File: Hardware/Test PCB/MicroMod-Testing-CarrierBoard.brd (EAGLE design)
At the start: 85.1 x 43.2 mm, 139 parts, among them J11 microSD, J12 SPI, J13 QWIIC_RIGHT_ANGLE, J15 Dedicated, J2 JTAG, J3 QWIIC_RIGHT_ANGLE, J6 MICROMOD-2222-C, J8 Dedicated, U2 MCP73831, U5 AP7361C-33

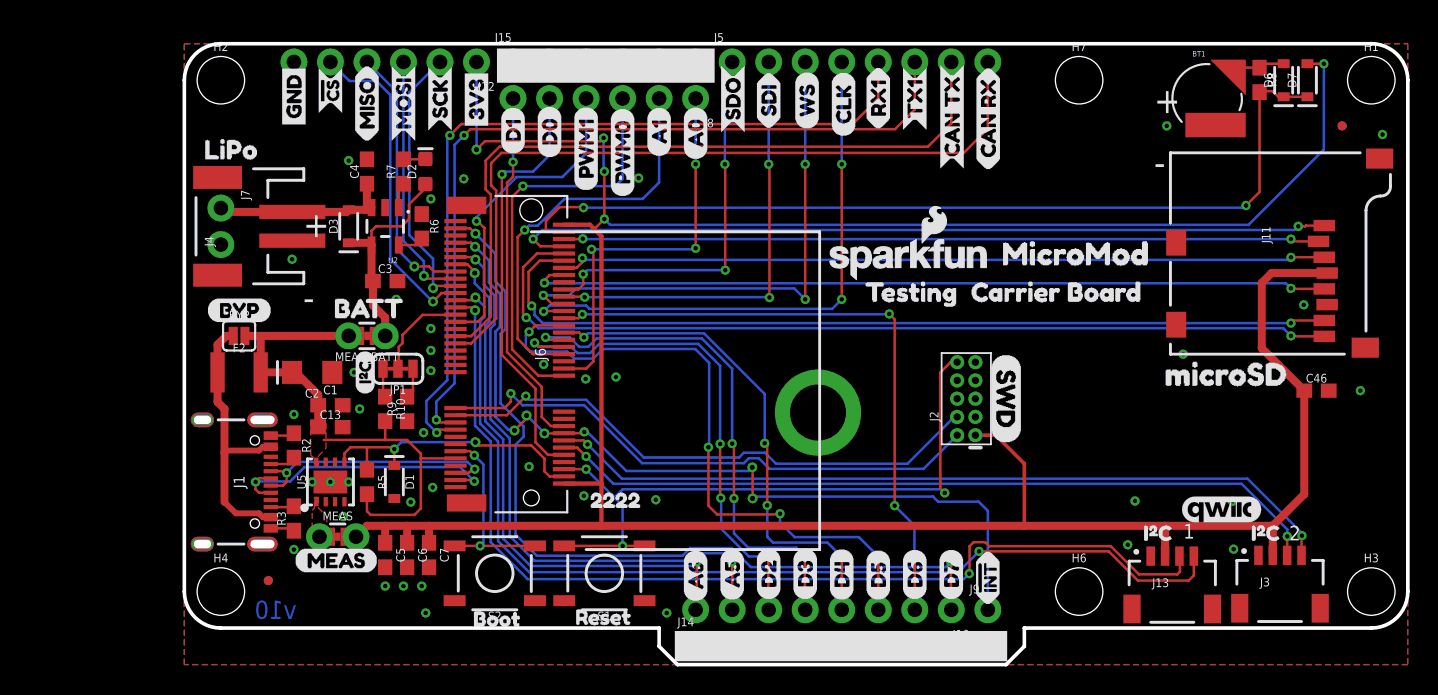
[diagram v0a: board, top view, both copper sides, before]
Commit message: Updates testing carrier board with all nets added and half of teh new ones added
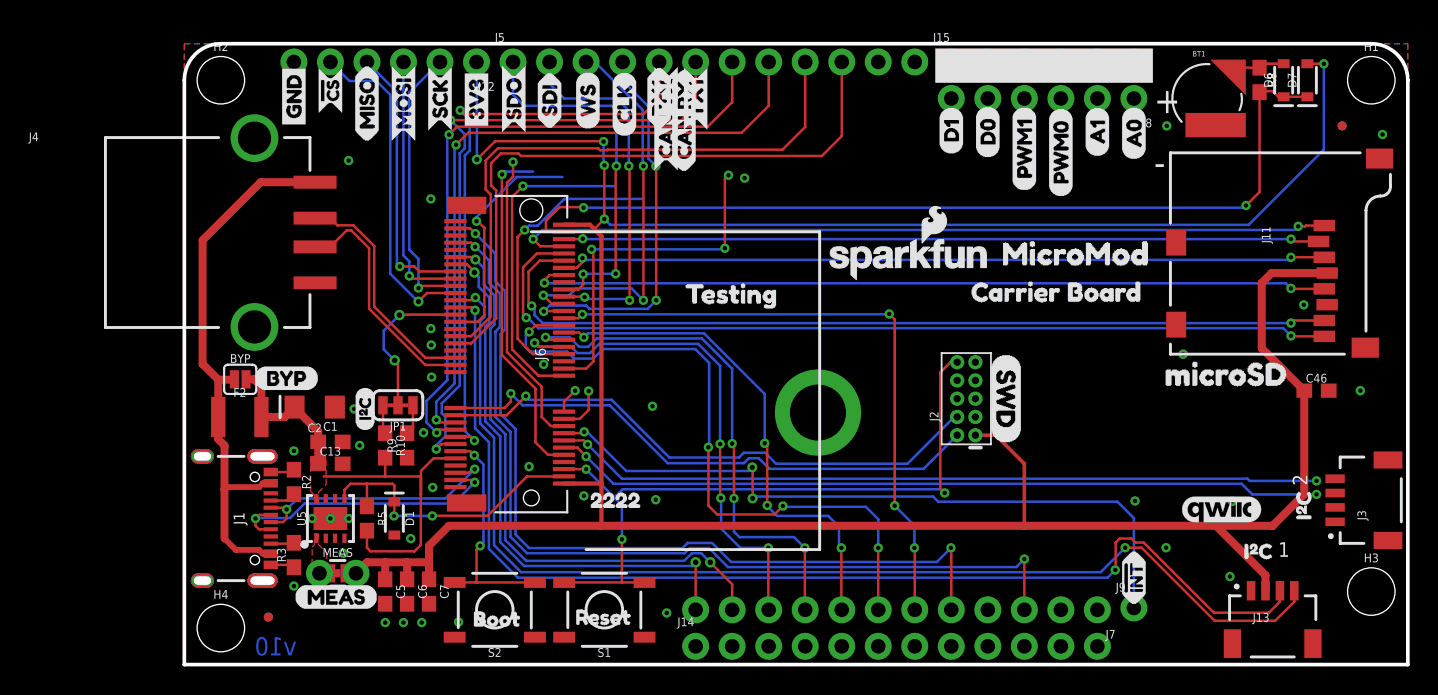
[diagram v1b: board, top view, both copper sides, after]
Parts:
- removed C3, C4: 4.7uF, SparkFun-Capacitors:0603
- removed D2: Yellow, SparkFun-LED:LED-0603
- removed D3: 3A/10V/280mV, SparkFun-DiscreteSemi:SOD-323
- removed H6, H7: STAND-OFF, SparkFun-Hardware:STAND-OFF
- removed J10: (no value), SparkFun-Connectors:1X08_NO_SILK
- removed MEAS_BATT: (no value), SparkFun-Jumpers:COMBO-JUMPER_2_NC_TRACE
- removed R6: 2.2k, SparkFun-Resistors:0603
- removed R7: 1k, SparkFun-Resistors:0603
- removed U$1, U$67: (no value), bottom PTH:A51
- removed U$11, U$69: (no value), bottom PTH:D22
- removed U$17, U$70: (no value), bottom PTH:D33
- removed U$18, U$71: (no value), bottom PTH:D44
- removed U$20, U$72: (no value), bottom PTH:D55
- removed U$3, U$68: (no value), bottom PTH:A60
- removed U$30, U$73: (no value), bottom PTH:D66
- removed U$32, U$74: (no value), bottom PTH:D77
- removed U$33: (no value), buzzard_labels (9):LIPO0
- removed U$56: (no value), buzzard_labels:BATT0
- removed U2: MCP73831, SparkFun-IC-Power:SOT23-5
- J14: device SparkFun-Connectors:1X09_NO_SILK -> SparkFun-Connectors:1X12_NO_SILK
- J4: value (none) -> USB_A_SMT_FEMALE; device SparkFun-Connectors:JST-2-SMD -> SparkFun-Connectors:USB-A-S-SILK-FEMALE
- J5: device SparkFun-Connectors:1X08_NO_SILK -> SparkFun-Connectors:1X12_NO_SILK
- J7: device SparkFun-Connectors:1X02_NO_SILK -> SparkFun-Connectors:1X12_NO_SILK
- moved J7 67.1 mm to (63.5, 3.81), turned to 180 degrees
- moved J15 30.5 mm to (53.3, 41.9)
- moved J8 30.5 mm to (66.0, 39.4)
- moved U$12 30.5 mm to (53.3, 35.4)
- moved U$13 30.5 mm to (53.3, 35.4)
- moved U$14 30.5 mm to (55.9, 35.2)
- moved U$16 30.5 mm to (55.9, 35.2)
- moved U$43 30.5 mm to (66.0, 35.1)
- moved U$44 30.5 mm to (66.0, 35.1)
- moved U$15 30.5 mm to (58.4, 32.9)
- moved U$59 30.5 mm to (61.0, 32.5)
- moved U$60 30.5 mm to (61.0, 32.5)
- moved U$61 30.5 mm to (58.4, 32.9)
- moved U$57 30.5 mm to (63.5, 35.3)
- moved U$58 30.5 mm to (63.5, 35.3)
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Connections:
- net USB_D+ renamed USB_P
- net USB_D- renamed USB_N
- removed net 5V: C3.1, D2.A, D3.C, MEAS_BATT.1, MEAS_BATT.3, U2.4
- removed net A5: J10.7, J6.65
- removed net A6: J10.8, J6.63
- removed net CHG_LED: R7.1, U2.1
- removed net D2: J10.6, J6.40
- removed net D3: J10.5, J6.42
- removed net D4: J10.4, J6.44
- removed net D5: J10.3, J6.46
- removed net D6: J10.2, J6.48
- removed net D7: J10.1, J6.73
- removed net D8/!INT: J6.16, J6.69, J9.1
- removed net N$4: D2.C, R7.2
- removed net N$7: R6.2, U2.5
- removed net V_BATT: C4.1, D3.A, J4.2, J7.1, U2.3
- new net CTS1: J5.5, J6.15
- new net G0: J6.40, J7.10
- new net G1: J6.42, J7.9
- new net G10/ADC_P: J6.63, J7.12
- new net G11: J6.8, J7.1
- new net G2: J6.44, J7.8
- new net G3: J6.46, J7.7
- new net G4: J6.48, J7.6
- new net G5: J6.73, J7.5
- new net G6: J6.71, J7.4
- new net G7: J6.69, J7.3
- new net G8: J6.67, J7.2
- new net G9/ADC_N: J6.65, J7.11
- new net I2C_!INT: J6.16, J9.1
- new net MCLK: J6.58
- new net RTS1: J5.6, J6.13
- new net RX2: J5.12, J6.20
- new net TX2: J5.11, J6.22
- new net USBHOST_N: J4.D-, J6.37
- new net USBHOST_P: J4.D+, J6.35
- net CAN_RXI: now also J5.10; no longer J5.8
- net CAN_TXO: now also J5.9; no longer J5.7
- net GND: now also J14.10, J14.11, J14.12, J4.GND, J4.SHLD1, J4.SHLD2; no longer C3.2, C4.2, J4.1, J7.2, R6.1, U2.2
- net RX1: now also J5.8; no longer J5.6
- net TX1: now also J5.7; no longer J5.5
- net VIN: no longer MEAS_BATT.2, MEAS_BATT.4
- net V_USB: now also J4.VBUS
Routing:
- net G7: track 0.00 -> 63.6 mm, vias 0 -> 2
- net D8/!INT: track 60.7 -> 0.00 mm, vias 7 -> 0
- net G5: track 0.00 -> 60.0 mm, vias 0 -> 2
- net D7: track 59.5 -> 0.00 mm, vias 2 -> 0
- net I2C_!INT: track 0.00 -> 50.0 mm, vias 0 -> 3
- net G3: track 0.00 -> 46.5 mm, vias 0 -> 4
- net RTS1: track 0.00 -> 46.3 mm, vias 0 -> 2
- net D5: track 44.9 -> 0.00 mm, vias 4 -> 0
- net G4: track 0.00 -> 44.0 mm, vias 0 -> 4
- net D6: track 44.0 -> 0.00 mm, vias 4 -> 0
- net A5: track 42.1 -> 0.00 mm, vias 2 -> 0
- net CTS1: track 0.00 -> 42.0 mm, vias 0 -> 2
- net G9/ADC_N: track 0.00 -> 41.3 mm, vias 0 -> 2
- net G10/ADC_P: track 0.00 -> 39.0 mm, vias 0 -> 2
- net A6: track 38.9 -> 0.00 mm, vias 2 -> 0
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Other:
- outline, holes or cut-outs redrawn

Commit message: Finishes routing board
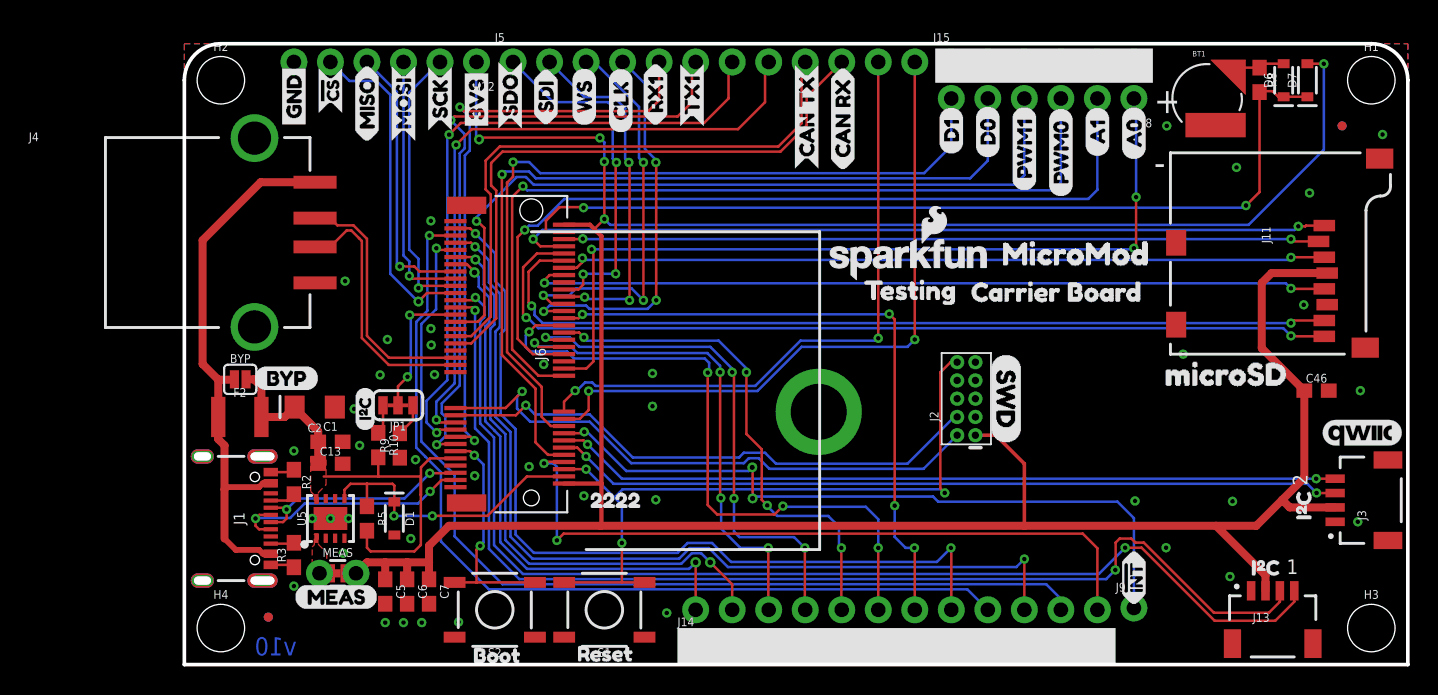
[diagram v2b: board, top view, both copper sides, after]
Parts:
- removed LOGO4: SFE_LOGO_NAME_FLAME.1_INCH, SparkFun-Aesthetics:SFE_LOGO_NAME_FLAME_.1
- removed U$22: (no value), buzzard_labels (9):LOGGING4
- removed U$4: (no value), buzzard_labels (9):DATA3
- moved U$64 38.1 mm to (66.4, 25.7)
- moved U$46 12.4 mm to (46.2, 26.0)
- moved LOGO2 11.1 mm to (81.9, 16.1)
- moved U$34 11.0 mm to (45.8, 34.3)
- moved U$48 11.0 mm to (45.8, 34.3)
- moved U$36 9.78 mm to (43.3, 34.4)
- moved U$54 9.78 mm to (43.3, 34.4)
- moved U$2 2.54 mm to (26.4, 0.76)
- moved H3 2.54 mm to (82.5, 2.54)
- moved U$19 2.54 mm to (19.2, 0.64)
- moved U$75 1.25 mm to (73.3, 6.73)
- moved R9 0.51 mm to (15.0, 15.2)
- moved R10 0.48 mm to (13.5, 15.3)
- moved U$25 0.36 mm to (32.8, 37.5)
- moved U$29 0.36 mm to (32.8, 37.5)
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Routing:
- net G8: track 0.00 -> 67.5 mm, vias 0 -> 1
- net G6: track 0.00 -> 64.2 mm, vias 0 -> 1
- net G11: track 0.00 -> 50.1 mm, vias 0 -> 2
- net RX2: track 3.29 -> 46.8 mm, vias 1 -> 2
- net TX2: track 1.78 -> 43.8 mm, vias 1 -> 2
- net A1: track 20.5 -> 58.8 mm
- net PWM1: track 16.4 -> 54.4 mm
- net PWM0: track 22.5 -> 59.6 mm
- net D0: track 24.2 -> 60.8 mm
- net D1: track 20.7 -> 55.6 mm
- net A0: track 24.6 -> 58.4 mm
- net USB_N: track 18.7 -> 15.8 mm
- net USB_P: track 20.5 -> 17.8 mm
- net CAN_RXI: track 45.0 -> 43.0 mm
- net USBHOST_N: track 16.3 -> 17.7 mm
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
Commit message: Adds labels to testing carrier board
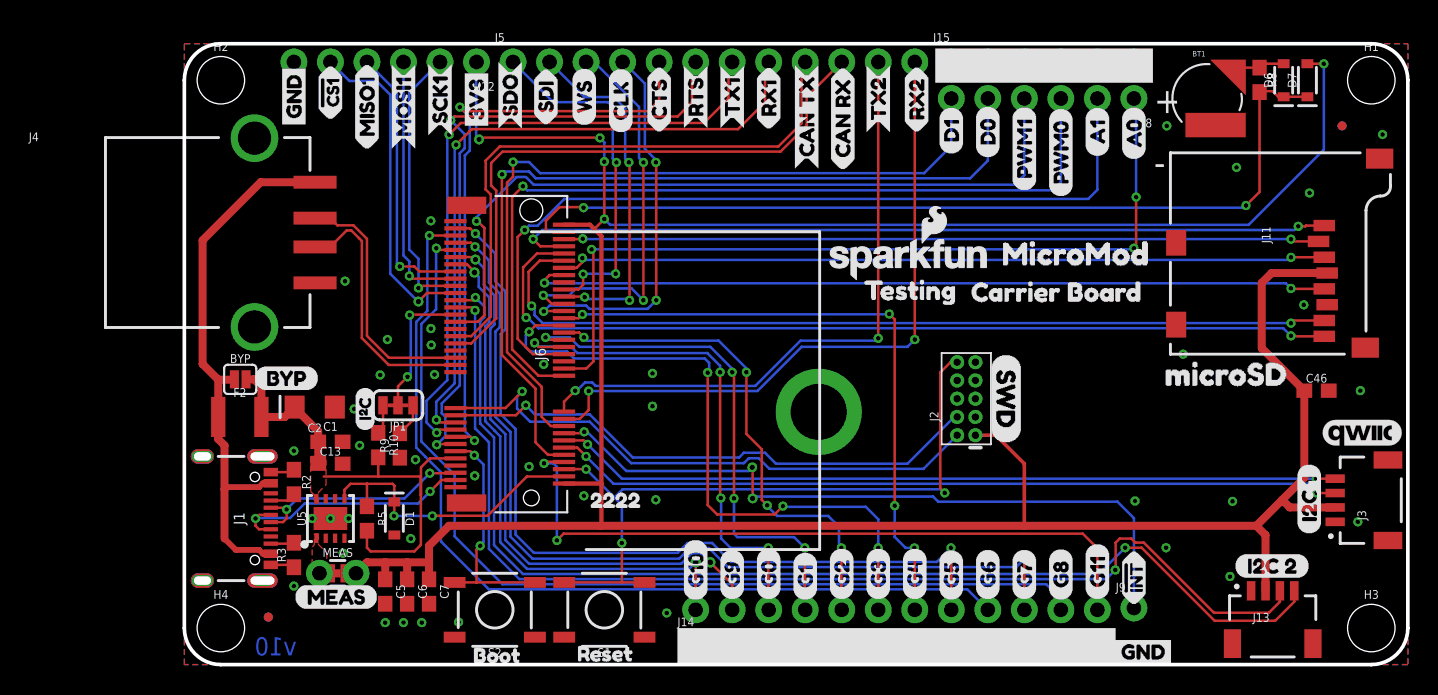
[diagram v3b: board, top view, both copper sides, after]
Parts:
- added U$1, U$89: (no value), Bus Labels:G00
- added U$11, U$86: (no value), Bus Labels:G33
- added U$17, U$85: (no value), Bus Labels:G44
- added U$18, U$84: (no value), Bus Labels:G55
- added U$20, U$83: (no value), Bus Labels:G66
- added U$22, U$82: (no value), Bus Labels:G77
- added U$3, U$88: (no value), Bus Labels:G11
- added U$30, U$80: (no value), Bus Labels:G118
- added U$32, U$81: (no value), Bus Labels:G811
- added U$33: (no value), Bus Labels:G1010
- added U$4, U$87: (no value), Bus Labels:G22
- added U$56: (no value), G9:G90
- added U$67: (no value), Extra I2C Lables:I2C_10
- added U$68: (no value), Extra I2C Lables:I2C_21
- added U$69, U$70: (no value), SERIAL2:RX23
- added U$71, U$72: (no value), SERIAL2:TX22
- added U$73: (no value), SparkFun-Buzzard:GND_P
- added U$74: (no value), SPI1:#CS13
- added U$77: (no value), SPI1:SCK12
- added U$78: (no value), SERIAL2:CTS0
- added U$79: (no value), SERIAL2:RTS1
- U$10: device SparkFun-Buzzard:!CS_O -> SPI1:MISO10
- U$49: device SparkFun-Buzzard:SCK_O -> SPI1:MOSI11
- U$50: device SparkFun-Buzzard:MOSI_O -> SPI1:SCK12
- U$51: device SparkFun-Buzzard:MISO_I -> SERIAL2:CTS0
- U$52: device SparkFun-Buzzard:!CS_O -> SERIAL2:RTS1
- U$7: device SparkFun-Buzzard:MOSI_O -> CAM_ADC:ADC_D##CAM_HSYNC0
- U$75: device SparkFun-Buzzard:I2C_TO -> SPI1:MISO10
- U$76: device SparkFun-Buzzard:I2C_TO -> SPI1:MOSI11
- U$8: device SparkFun-Buzzard:MISO_I -> CAM_ADC:ADC_D##CAM_VSYNC1
- U$9: device SparkFun-Buzzard:SCK_O -> SPI1:#CS13
- moved U$76 68.1 mm to (15.2, 35.8), flipped to the bottom
- moved U$75 67.2 mm to (12.7, 35.8), flipped to the bottom, turned to 90 degrees
- moved U$7 39.2 mm to (38.1, 4.45), flipped to the bottom
- moved U$8 39.2 mm to (35.6, 4.45), flipped to the bottom
- moved U$52 25.4 mm to (35.6, 37.2), flipped to the top
- moved U$51 20.3 mm to (33.0, 37.0), flipped to the top
- moved U$25 7.88 mm to (40.6, 37.2)
- moved U$29 7.88 mm to (40.6, 37.2)
- moved U$9 7.65 mm to (10.2, 37.7)
- moved U$10 3.42 mm to (12.7, 35.8)
- moved U$49 2.84 mm to (15.2, 35.8), flipped to the top
- moved U$31 2.80 mm to (38.1, 37.2)
- moved U$41 2.80 mm to (38.1, 37.2)
- moved U$50 2.57 mm to (17.8, 36.7), flipped to the top
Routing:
- net 3.3V: track 217.6 -> 216.4 mm
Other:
- outline, holes or cut-outs redrawn
- board text added: "Elias Santistevan"
- board text removed: "1"
- board text removed: "2"
